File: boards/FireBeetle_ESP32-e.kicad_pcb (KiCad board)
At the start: 2 copper layers, 63.5 x 48.3 mm, 10 parts

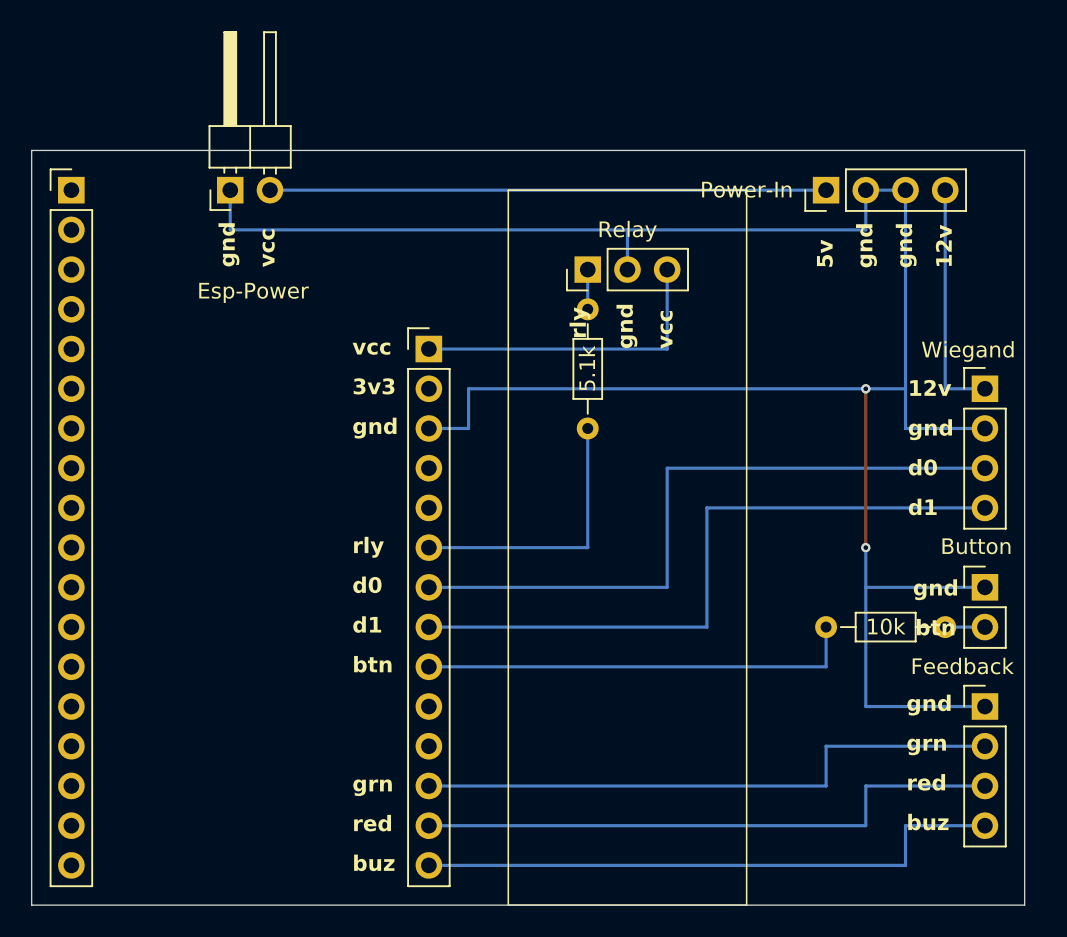
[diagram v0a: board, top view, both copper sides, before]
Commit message: Fixed misbehaving firebeetle pins, adjusted firebeetle board for new pins
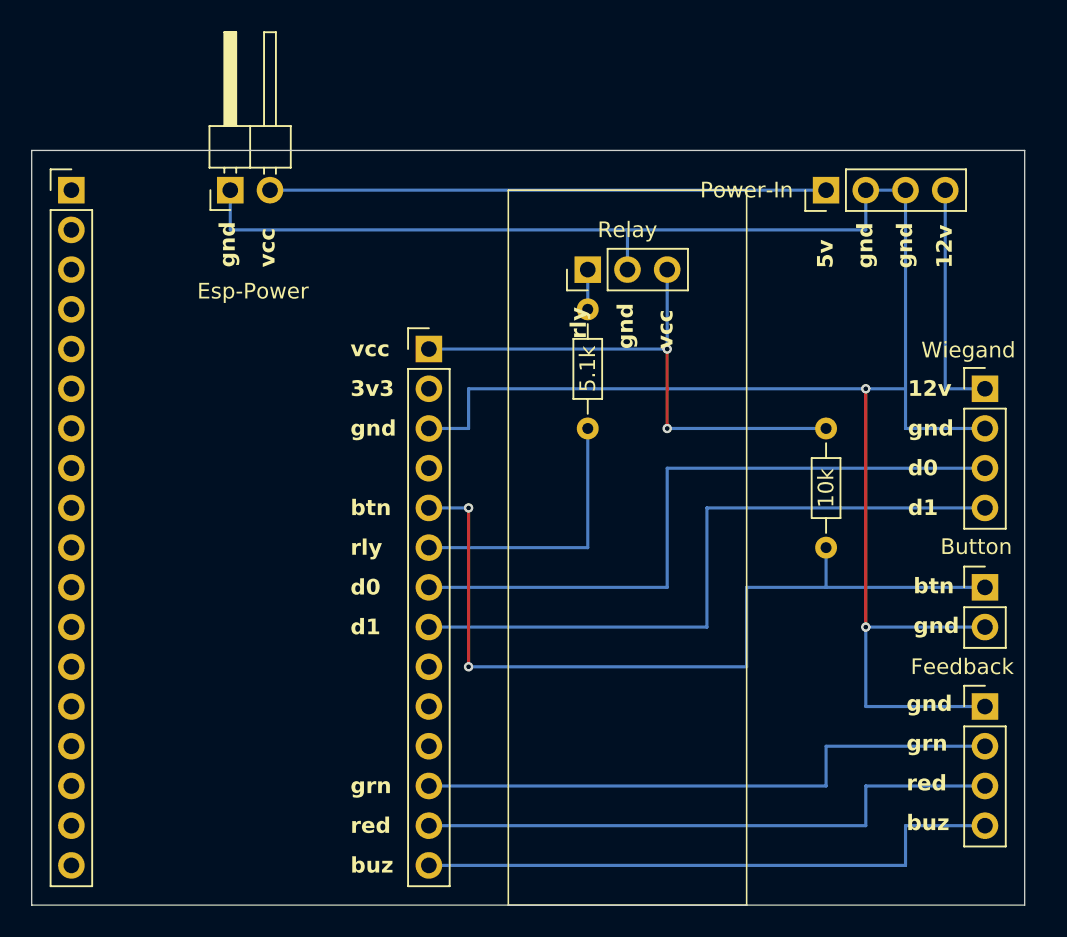
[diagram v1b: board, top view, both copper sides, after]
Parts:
- moved 10k 5.08 mm to (73.7, 48.3), turned to 90 degrees
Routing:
- net (no net): track 462.3 -> 500.4 mm, vias 2 -> 6

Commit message: Modified board, added pullup setting to button pins, changed http 200 to constant
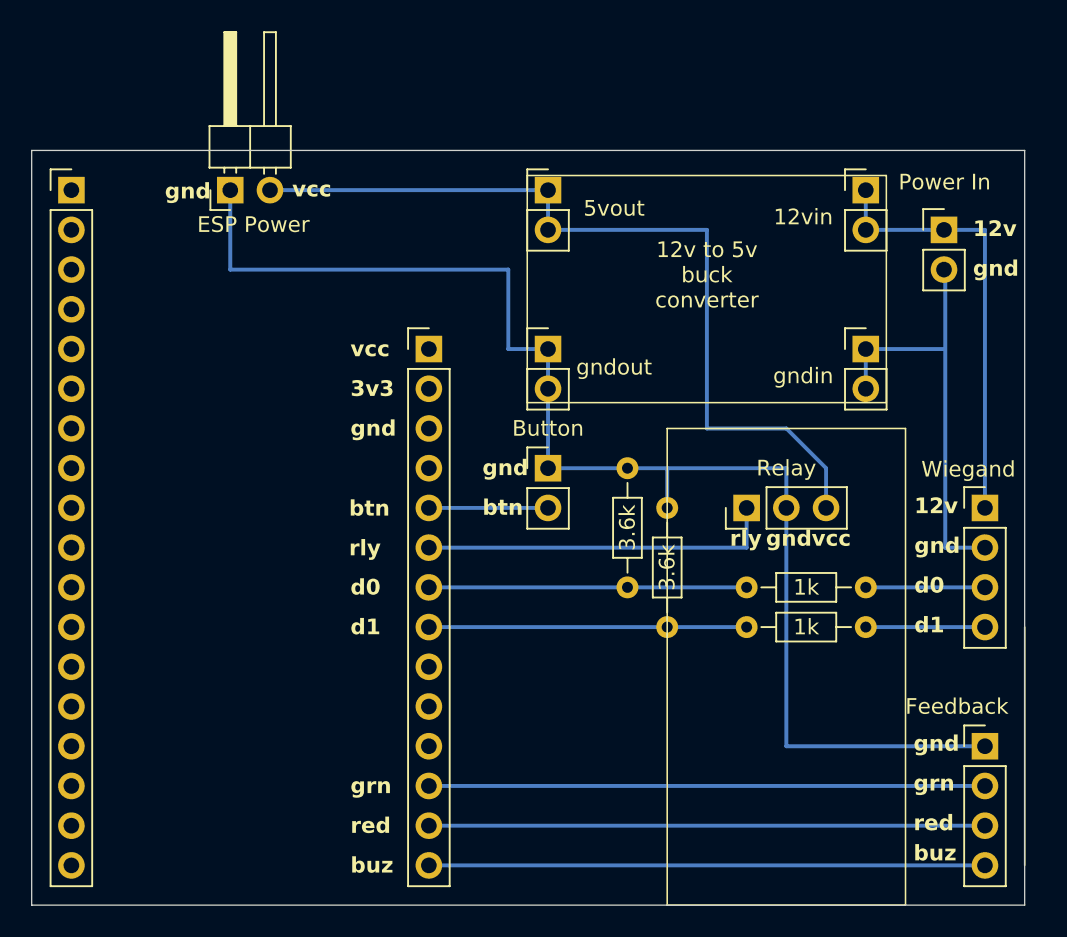
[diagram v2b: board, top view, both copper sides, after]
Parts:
- removed 10k, 5.1k: R_Axial_DIN0204_L3.6mm_D1.6mm_P7.62mm_Horizontal, Resistor_THT:R_Axial_DIN0204_L3.6mm_D1.6mm_P7.62mm_Horizontal
- removed Esp-Power: PinHeader_1x02_P2.54mm_Horizontal, Connector_PinHeader_2.54mm:PinHeader_1x02_P2.54mm_Horizontal
- removed Power-In: PinHeader_1x04_P2.54mm_Vertical, Connector_PinHeader_2.54mm:PinHeader_1x04_P2.54mm_Vertical
- added 12vin: PinHeader_1x02_P2.54mm_Vertical, Connector_PinHeader_2.54mm:PinHeader_1x02_P2.54mm_Vertical, F.Cu at (76.2, 25.4)
- added 1k: R_Axial_DIN0204_L3.6mm_D1.6mm_P7.62mm_Horizontal, Resistor_THT:R_Axial_DIN0204_L3.6mm_D1.6mm_P7.62mm_Horizontal, F.Cu at (76.2, 53.3)
- added 1k: R_Axial_DIN0204_L3.6mm_D1.6mm_P7.62mm_Horizontal, Resistor_THT:R_Axial_DIN0204_L3.6mm_D1.6mm_P7.62mm_Horizontal, F.Cu at (76.2, 50.8)
- added 3.6k: R_Axial_DIN0204_L3.6mm_D1.6mm_P7.62mm_Horizontal, Resistor_THT:R_Axial_DIN0204_L3.6mm_D1.6mm_P7.62mm_Horizontal, F.Cu at (63.5, 53.3)
- added 3.6k: R_Axial_DIN0204_L3.6mm_D1.6mm_P7.62mm_Horizontal, Resistor_THT:R_Axial_DIN0204_L3.6mm_D1.6mm_P7.62mm_Horizontal, F.Cu at (61.0, 50.8)
- added 5vout: PinHeader_1x02_P2.54mm_Vertical, Connector_PinHeader_2.54mm:PinHeader_1x02_P2.54mm_Vertical, F.Cu at (55.9, 25.4)
- added ESP Power: PinHeader_1x02_P2.54mm_Horizontal, Connector_PinHeader_2.54mm:PinHeader_1x02_P2.54mm_Horizontal, F.Cu at (35.6, 25.4)
- added Power In: PinHeader_1x02_P2.54mm_Vertical, Connector_PinHeader_2.54mm:PinHeader_1x02_P2.54mm_Vertical, F.Cu at (81.2, 27.9)
- added gndin: PinHeader_1x02_P2.54mm_Vertical, Connector_PinHeader_2.54mm:PinHeader_1x02_P2.54mm_Vertical, F.Cu at (76.2, 35.6)
- added gndout: PinHeader_1x02_P2.54mm_Vertical, Connector_PinHeader_2.54mm:PinHeader_1x02_P2.54mm_Vertical, F.Cu at (55.9, 35.6)
- moved Button 29.0 mm to (55.9, 43.2)
- moved Relay 18.3 mm to (68.6, 45.7)
- moved Wiegand 7.62 mm to (83.8, 45.7)
- moved Feedback 2.54 mm to (83.8, 61.0)
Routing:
- net (no net): track 500.4 -> 389.2 mm, vias 6 -> 0
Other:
- board text added: "12v to 5v buck converter"
- board text removed: "5v"

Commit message: Updated Board design for Firebeetle
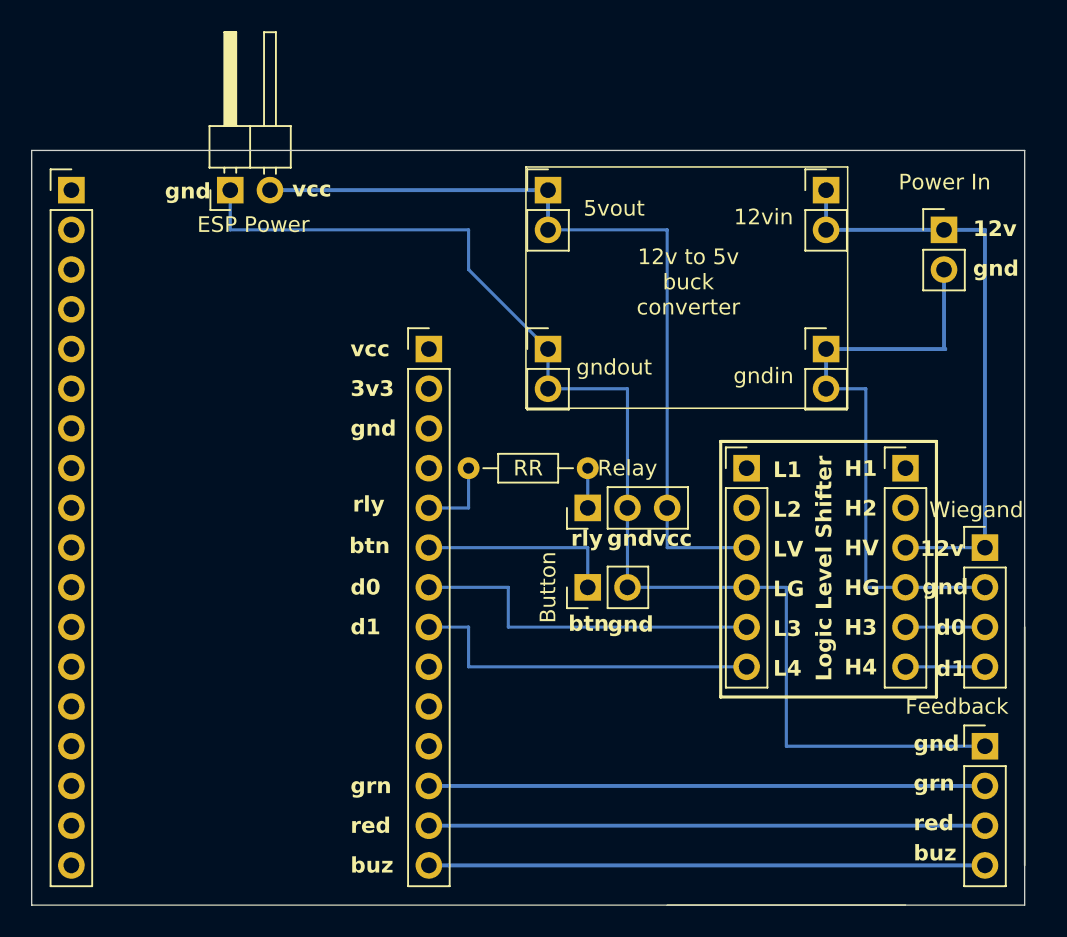
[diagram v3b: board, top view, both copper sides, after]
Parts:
- removed 1k (x2), 3.6k (x2): R_Axial_DIN0204_L3.6mm_D1.6mm_P7.62mm_Horizontal, Resistor_THT:R_Axial_DIN0204_L3.6mm_D1.6mm_P7.62mm_Horizontal
- added HV: PinHeader_1x06_P2.54mm_Vertical, Connector_PinHeader_2.54mm:PinHeader_1x06_P2.54mm_Vertical, F.Cu at (78.7, 43.2)
- added LV: PinHeader_1x06_P2.54mm_Vertical, Connector_PinHeader_2.54mm:PinHeader_1x06_P2.54mm_Vertical, F.Cu at (68.6, 43.2)
- added RR: R_Axial_DIN0204_L3.6mm_D1.6mm_P7.62mm_Horizontal, Resistor_THT:R_Axial_DIN0204_L3.6mm_D1.6mm_P7.62mm_Horizontal, F.Cu at (50.8, 43.2)
- moved Relay 10.2 mm to (58.4, 45.7)
- moved Button 8.03 mm to (58.4, 50.8), turned to 90 degrees
- moved 12vin 2.54 mm to (73.7, 25.4)
- moved gndin 2.54 mm to (73.7, 35.6)
- moved Wiegand 2.54 mm to (83.8, 48.3)
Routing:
- net (no net): track 389.2 -> 395.5 mm
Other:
- board text added: "H1"
- board text added: "H2"
- board text added: "H3"
- board text added: "H4"
- board text added: "HG"
- board text added: "HV"
- board text added: "L1"
- board text added: "L2"
- board text added: "L3"
- board text added: "L4"
- board text added: "LG"
- board text added: "LV"
- board text added: "Logic Level Shifter"
